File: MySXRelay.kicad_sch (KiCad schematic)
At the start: 50 parts, among them K2 FH44L-1AT-L1-DC5V, Q1 2N7002, U1 MIC4427, U2 BL0942, U3 BP2525X, U4 Si8642BB-B-IS1

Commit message: finished schematic
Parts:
- C1, C13, C14: footprint Capacitor_SMD:C_0603_1608Metric -> Capacitor_SMD:C_0402_1005Metric
- C5: value 4.7u/400V -> 2.2u/400V; footprint Capacitor_THT:CP_Radial_D10.0mm_P5.00mm -> Capacitor_THT:CP_Radial_D8.0mm_P3.50mm
- C6: value 680u/10V -> 470u/10V
- L1: value 330m/300mA -> 330u; footprint Inductor_THT:L_Radial_D7.0mm_P3.00mm -> Inductor_SMD:L_1812_4532Metric_Pad1.30x3.40mm_HandSolder
- TH1: value 50mA -> ERF-LX005V2
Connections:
- net D10_A4: now also X1.16 (Pin_16); no longer X1.15 (Pin_15)
- net D11_MOSI_TX: now also X1.17 (Pin_17); no longer X1.18 (Pin_18)
- net D12_MISO_RX: now also X1.18 (Pin_18); no longer X1.17 (Pin_17)
- net D13_SCK: now also X1.19 (Pin_19); no longer X1.20 (Pin_20)
- net D14_CS: now also X1.20 (Pin_20); no longer X1.19 (Pin_19)
- net D1_TX: now also X1.5 (Pin_5); no longer X1.6 (Pin_6)
- net D2_RX: now also X1.6 (Pin_6); no longer X1.5 (Pin_5)
- net D3_INT: now also X1.9 (Pin_9); no longer X1.10 (Pin_10)
- net D4_INT: now also X1.10 (Pin_10); no longer X1.9 (Pin_9)
- net D5_PWM: now also X1.11 (Pin_11); no longer X1.12 (Pin_12)
- net D6_PWM: now also X1.12 (Pin_12); no longer X1.11 (Pin_11)
- net D7_SCL: now also X1.13 (Pin_13); no longer X1.14 (Pin_14)
- net D8_SDA: now also X1.14 (Pin_14); no longer X1.13 (Pin_13)
- net D9_A3: now also X1.15 (Pin_15); no longer X1.16 (Pin_16)
- net GND: now also X1.4 (Pin_4); no longer X1.3 (Pin_3)
- net LEGACY_ID: now also X1.8 (Pin_8); no longer X1.7 (Pin_7)
- net RST: now also X1.7 (Pin_7); no longer X1.8 (Pin_8)
- net VCC: now also X1.2 (Pin_2); no longer X1.1 (Pin_1)
- net VCCIO: now also X1.3 (Pin_3); no longer X1.4 (Pin_4)
- net VRAW: now also X1.1 (Pin_1); no longer X1.2 (Pin_2)
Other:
- moved on the sheet: D3, D4, X1

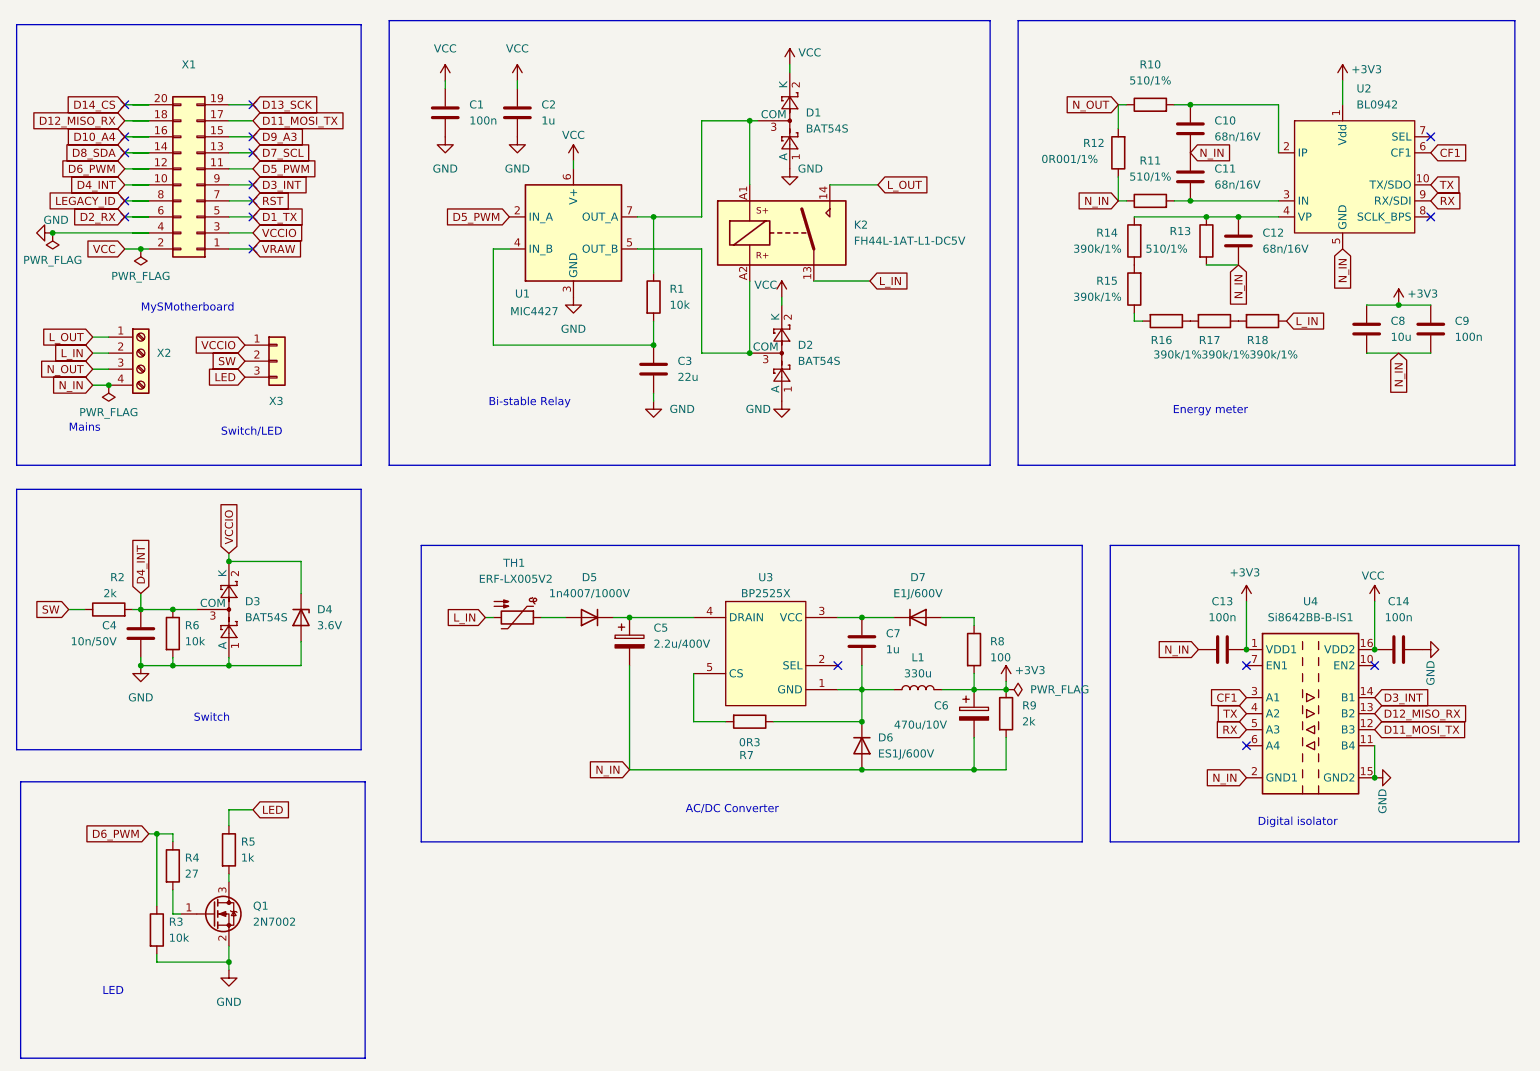
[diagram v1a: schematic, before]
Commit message: add LDO on mains power supply output
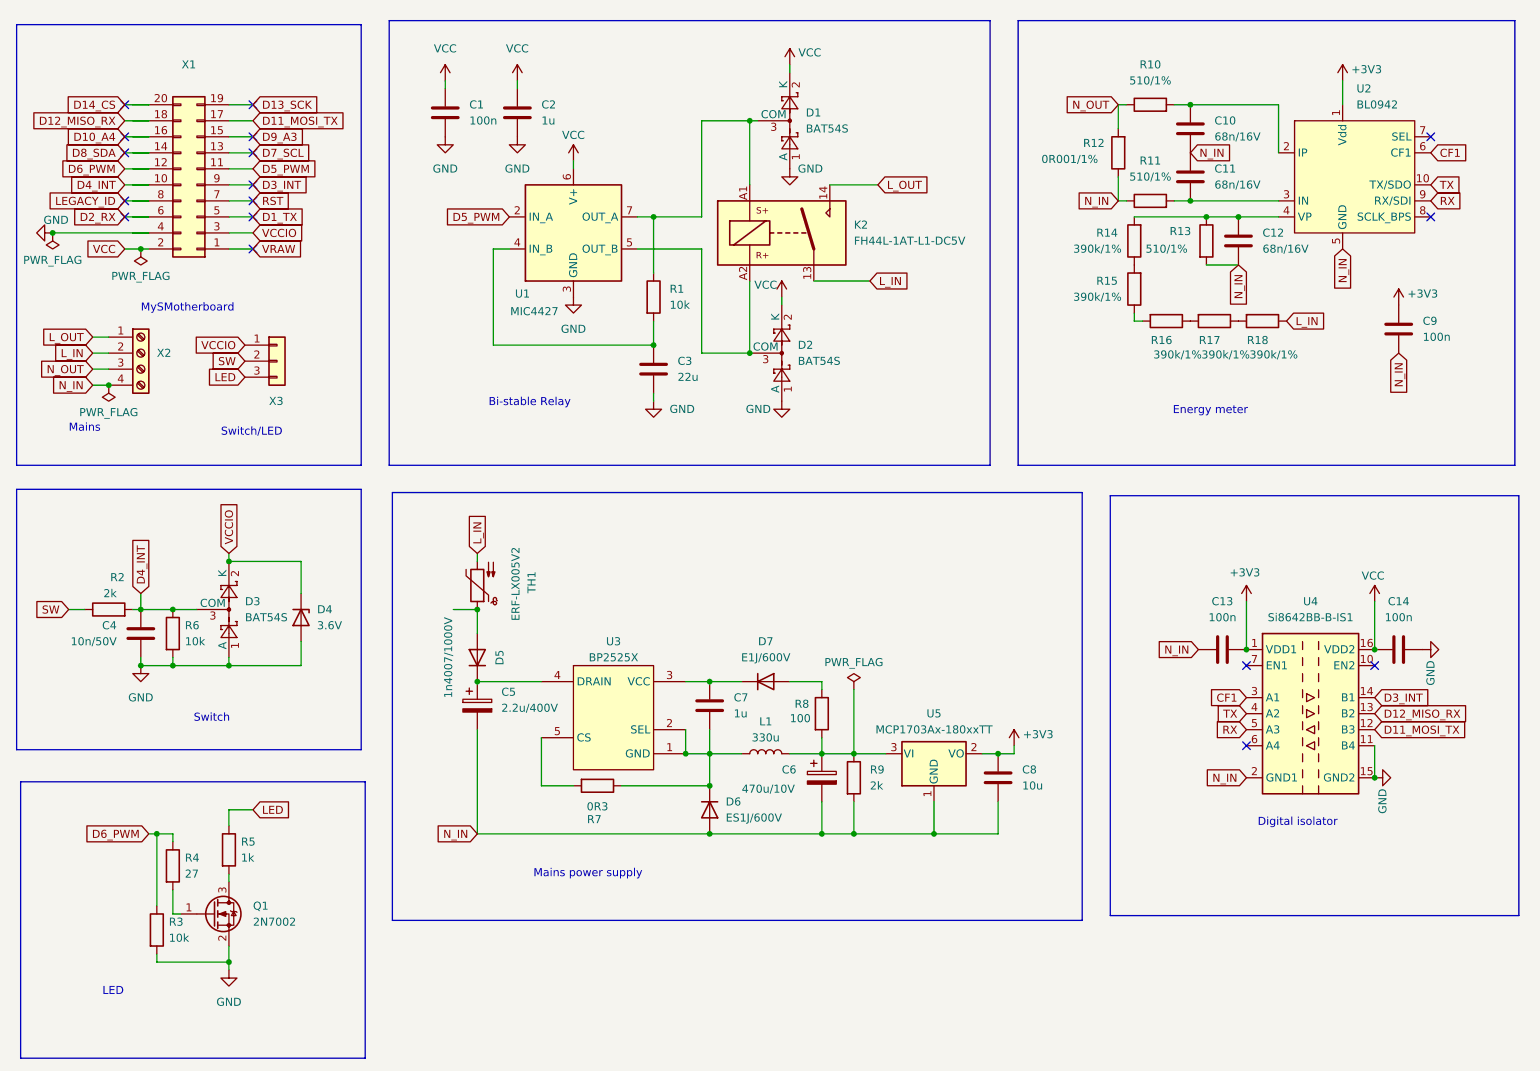
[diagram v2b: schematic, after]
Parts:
- added U5: MCP1703Ax-180xxTT, Package_TO_SOT_SMD:SOT-23, symbol Regulator_Linear:MCP1703Ax-180xxTT
- L1: footprint Inductor_SMD:L_1812_4532Metric_Pad1.30x3.40mm_HandSolder -> Inductor_THT:L_Radial_D7.0mm_P3.00mm
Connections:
- net +3V3: now also U5.2 (VO); no longer C6.1, L1.2, R8.2, R9.1
- net N_IN: now also U5.1 (GND)
- net at C7.2, D6.1 (K), L1.1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: now also U3.2 (SEL)
- new net: C6.1, L1.2, R8.2, R9.1, U5.3 (VI)
- no-connect marks 18 -> 17
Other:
- note added: "Mains power supply"
- note removed: "AC/DC Converter"
- moved on the sheet: C5, C6, C7, C8, C9, D5, D6, D7, L1, R7, R8, R9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

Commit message: setup PCS dimensions
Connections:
- net L_IN: now also X2.3 (Pin_3); no longer X2.2 (Pin_2)
- net L_OUT: now also X2.4 (Pin_4); no longer X2.1 (Pin_1)
- net N_IN: now also X2.1 (Pin_1); no longer X2.4 (Pin_4)
- net N_OUT: now also X2.2 (Pin_2); no longer X2.3 (Pin_3)
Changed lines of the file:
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@@
 	)
 	(junction
+		(at 36.83 71.12)
+		(diameter 0)
+		(color 0 0 0 0)
+	)
+	(junction
 		(at 132.08 125.73)
 		(diameter 0)
@@
 	)
 	(junction
-		(at 36.83 78.74)
-		(diameter 0)
-		(color 0 0 0 0)
-	)
-	(junction
 		(at 237.49 120.65)
 		(diameter 0)
@@
 	(wire
 		(pts
+			(xy 34.29 73.66) (xy 36.83 73.66)
+		)
+		(stroke
+			(width 0)
+			(type default)
+		)
+	)
+	(wire
+		(pts
 			(xy 144.78 27.94) (xy 144.78 29.21)
 		)
@@
 	(wire
 		(pts
-			(xy 34.29 71.12) (xy 36.83 71.12)
-		)
-		(stroke
-			(width 0)
-			(type default)
-		)
-	)
-	(wire
-		(pts
 			(xy 167.64 149.86) (xy 177.8 149.86)
 		)
@@
 	(wire
 		(pts
-			(xy 34.29 73.66) (xy 36.83 73.66)
-		)
-		(stroke
-			(width 0)
-			(type default)
-		)
-	)
-	(wire
-		(pts
 			(xy 130.81 73.66) (xy 130.81 57.15)
 		)
@@
 	(wire
 		(pts
+			(xy 34.29 71.12) (xy 36.83 71.12)
+		)
+		(stroke
+			(width 0)
+			(type default)
+		)
+	)
+	(wire
+		(pts
 			(xy 132.08 137.16) (xy 137.16 137.16)
 		)
@@
 	(wire
 		(pts
-			(xy 34.29 76.2) (xy 36.83 76.2)
-		)
-		(stroke
-			(width 0)
-			(type default)
-		)
-	)
-	(wire
-		(pts
 			(xy 118.11 142.24) (xy 132.08 142.24)
 		)
@@
 	(wire
 		(pts
-			(xy 34.29 78.74) (xy 36.83 78.74)
-		)
-		(stroke
-			(width 0)
-			(type default)
-		)
-	)
-	(wire
-		(pts
 			(xy 138.43 62.23) (xy 138.43 73.66)
 		)
@@
 	(wire
 		(pts
+			(xy 34.29 78.74) (xy 36.83 78.74)
+		)
+		(stroke
+			(width 0)
+			(type default)
+		)
+	)
+	(wire
+		(pts
 			(xy 55.88 57.15) (xy 59.69 57.15)
 		)
@@
 	(wire
 		(pts
+			(xy 34.29 76.2) (xy 36.83 76.2)
+		)
+		(stroke
+			(width 0)
+			(type default)
+		)
+	)
+	(wire
+		(pts
 			(xy 95.25 114.3) (xy 95.25 118.11)
 		)
@@
 	(text "Mains power supply"
 		(exclude_from_sim no)
-		(at 104.14 156.972 0)
+		(at 127 157.48 0)
 		(effects
 			(font
@@
 	(global_label "N_OUT"
 		(shape input)
-		(at 34.29 76.2 180)
+		(at 34.29 73.66 180)
 		(fields_autoplaced yes)
 		(effects
@@
 		)
 		(property "Intersheetrefs" "${INTERSHEET_REFS}"
-			(at 25.3781 76.2 0)
+			(at 25.3781 73.66 0)
 			(effects
 				(font
@@
 	(global_label "L_OUT"
 		(shape input)
-		(at 34.29 71.12 180)
+		(at 34.29 78.74 180)
 		(fields_autoplaced yes)
 		(effects
@@
 		)
 		(property "Intersheetrefs" "${INTERSHEET_REFS}"
-			(at 25.6805 71.12 0)
+			(at 25.6805 78.74 0)
 			(effects
 				(font
@@
 	(global_label "L_IN"
 		(shape input)
-		(at 34.29 73.66 180)
+		(at 34.29 76.2 180)
 		(fields_autoplaced yes)
 		(effects
@@
 		)
 		(property "Intersheetrefs" "${INTERSHEET_REFS}"
-			(at 27.3738 73.66 0)
+			(at 27.3738 76.2 0)
 			(effects
 				(font
@@
 	(global_label "N_IN"
 		(shape input)
-		(at 34.29 78.74 180)
+		(at 34.29 71.12 180)
 		(fields_autoplaced yes)
 		(effects
@@
 		)
 		(property "Intersheetrefs" "${INTERSHEET_REFS}"
-			(at 27.0714 78.74 0)
+			(at 27.0714 71.12 0)
 			(effects
 				(font
@@
 	(symbol
 		(lib_id "power:PWR_FLAG")
-		(at 36.83 78.74 180)
+		(at 36.83 71.12 0)
 		(unit 1)
 		(exclude_from_sim no)
@@
 		(dnp no)
 		(property "Reference" "#FLG02"
-			(at 36.83 80.645 0)
+			(at 36.83 69.215 0)
 			(effects
 				(font
@@
 		)
 		(property "Value" "PWR_FLAG"
-			(at 36.83 83.058 0)
+			(at 36.83 66.802 0)
 			(effects
 				(font
@@
 		)
 		(property "Footprint" ""
-			(at 36.83 78.74 0)
+			(at 36.83 71.12 0)
 			(effects
 				(font
@@
 		)
 		(property "Datasheet" "~"
-			(at 36.83 78.74 0)
+			(at 36.83 71.12 0)
 			(effects
 				(font
@@
 		)
 		(property "Description" "Special symbol for telling ERC where power comes from"
-			(at 36.83 78.74 0)
+			(at 36.83 71.12 0)
 			(effects
 				(font

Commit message: WIP
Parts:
- removed K2: FH44L-1AT-L1-DC5V, Relay_THT:Relay_SPST_Panasonic_ADW11, symbol Relay:Relay_SPST_Latching_1coil
- added K1: FH44L-1AT-L1-DC5V, MySXRelay:RELAY-TH_FH44L-1AT-L1-DC5V, symbol MySXRelay:Relay_SPST_Latching_1coil
- X2: footprint TerminalBlock_Phoenix:TerminalBlock_Phoenix_MKDS-1,5-4-5.08_1x04_P5.08mm_Horizontal -> MySXRelay:MSTB_2,5_4-G
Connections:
- net L_IN: now also K1.13
- net L_OUT: now also K1.14
- net at D2.3 (COM), U1.5 (OUT_B): now also K1.A2
- net at D1.3 (COM), R1.1, U1.7 (OUT_A): now also K1.A1
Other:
- moved on the sheet: D5, TH1

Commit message: PCB WIP
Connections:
- net VCCIO is gone; now on net VCC: D3.2 (K), D4.1 (K), X1.3 (Pin_3), X3.1 (Pin_1)
- net L_IN: now also K1.14, X2.4 (Pin_4); no longer K1.13, X2.3 (Pin_3)
- net L_OUT: now also K1.13, X2.3 (Pin_3); no longer K1.14, X2.4 (Pin_4)

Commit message: WIP PCB
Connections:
- net N_IN: now also X2.2 (Pin_2); no longer X2.1 (Pin_1)
- net N_OUT: now also X2.1 (Pin_1); no longer X2.2 (Pin_2)

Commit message: PCB placment and routing finished
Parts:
- added X4: ~, Connector_PinSocket_2.54mm:PinSocket_1x04_P2.54mm_Vertical, symbol Connector_Generic:Conn_01x04
- added X5: ~, MySXRelay:JST-XH_S_4P-2.54MM-PIN1-RIGHT, symbol Connector_Generic:Conn_01x04
- X3: footprint TerminalBlock_Phoenix:TerminalBlock_Phoenix_MPT-0,5-3-2.54_1x03_P2.54mm_Horizontal -> MySXRelay:JST-XH_S_3P-2.54MM
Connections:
- net LED: now also X3.1 (Pin_1); no longer X3.3 (Pin_3)
- net VCC: now also X3.3 (Pin_3); no longer X3.1 (Pin_1)
- new net: X4.1 (Pin_1), X5.1 (Pin_1)
- new net: X4.2 (Pin_2), X5.2 (Pin_2)
- new net: X4.3 (Pin_3), X5.3 (Pin_3)
- new net: X4.4 (Pin_4), X5.4 (Pin_4)
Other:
- moved on the sheet: X1, X2, X3
